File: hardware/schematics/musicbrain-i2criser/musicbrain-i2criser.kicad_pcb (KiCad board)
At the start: 2 copper layers, 28 x 80 mm, 2 parts, among them J1 BUS, J2 NAAR FRONT

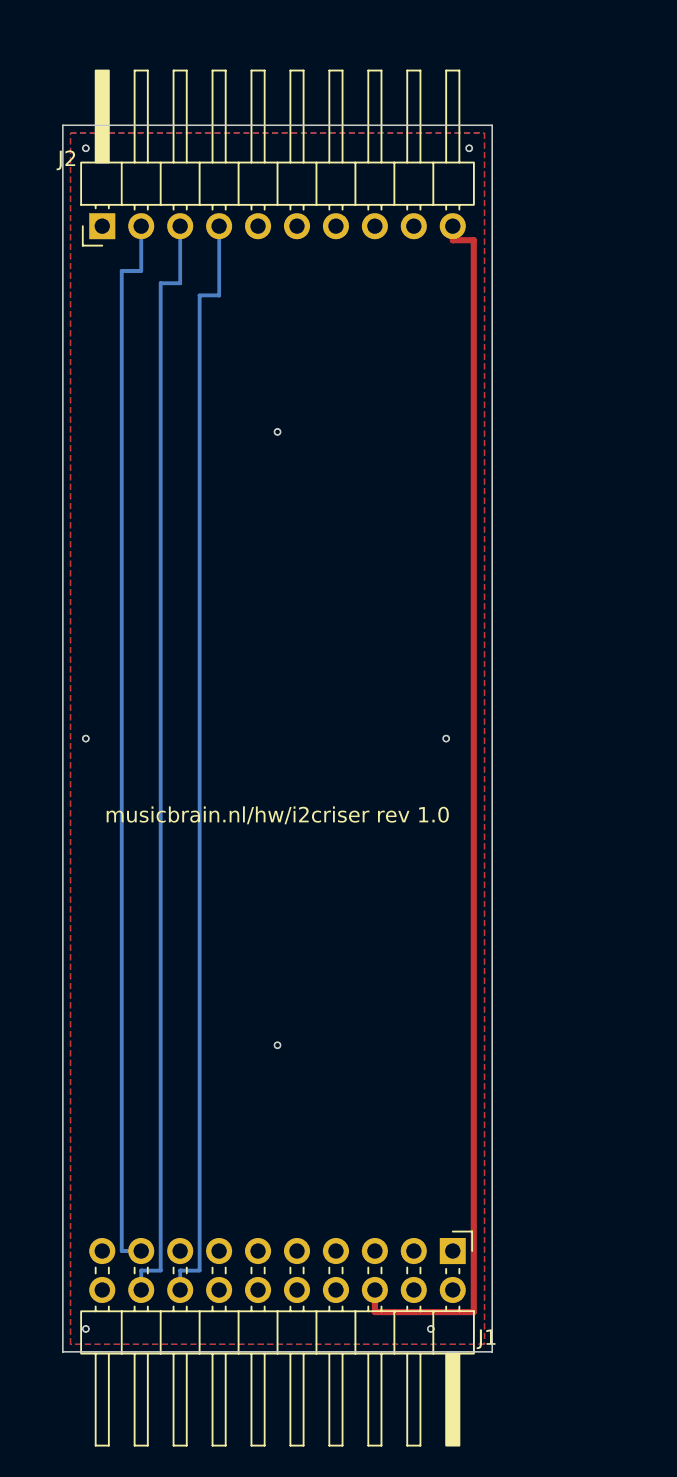
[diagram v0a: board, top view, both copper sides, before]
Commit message: Gen 2 stap 2+3a: bus.py + i2criser rev 2.0 (2x12, H=50) DRC 0/0
bus.py = één bron van waarheid voor bus-generatie 2 (spiegel van
spi-bus-spec v2.0): H=50, kaartbreedte 80, slotsteek 20,32, de 24-pins
SLOT-map, de 2x12-footprints en de front-standaard. Generators tikken de
pinout niet meer zelf over.

i2criser rev 2.0 = eerste bord op gen 2 (dom = snelste validatie van de
keten): 40x50 (de 2x12 spant 27,94 -> 28 mm was te smal), J1 2x12, J2 1x10
ongewijzigd. Routing-les: laan-volgorde is kritisch (SDA komt van de kolom
waar SCL naartoe moet -> SDA jogt meteen westwaarts); +3V3 gebruikt de
4 mm vrije strook zuid van J1 i.p.v. de krappe rijcorridor.
ERC 0 / netcheck OK / DRC 0/0.

Co-Authored-By: Claude Fable 5 <noreply@anthropic.com>
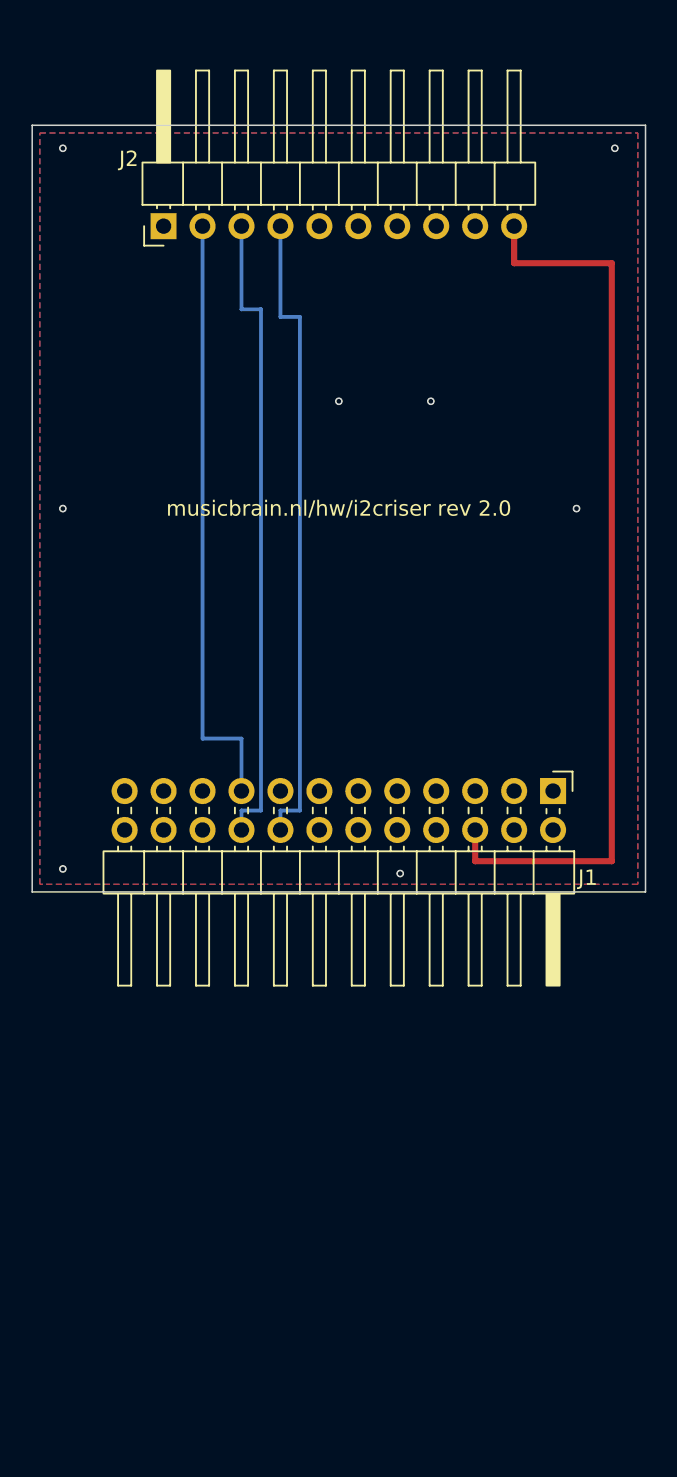
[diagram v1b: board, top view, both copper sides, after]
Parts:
- J1: footprint Connector_PinHeader_2.54mm:PinHeader_2x10_P2.54mm_Horizontal -> Connector_PinHeader_2.54mm:PinHeader_2x12_P2.54mm_Horizontal
- moved J1 30.7 mm to (134.0, 143.4)
- moved J2 4.00 mm to (108.6, 106.6)
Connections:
- J1 pad 20: (no net) -> GND
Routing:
- net /SCL: track 71.9 -> 41.9 mm
- net /IRQ: track 71.9 -> 41.9 mm
- net /SDA: track 69.4 -> 39.4 mm
- net +3V3: track 80.1 -> 58.7 mm
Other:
- board size 28 x 80 mm -> 40 x 50 mm
- board text added: "musicbrain.nl/hw/i2criser rev 2.0"
- board text removed: "musicbrain.nl/hw/i2criser rev 1.0"

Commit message: Release-archief rel-v0.2 per bord + paneel-inzet-fix (vondst Mark)
rel-v0.2/: de laatste gen-1-stand (2x10, H=80) van elk bord als bevroren
map naast de levende bestanden — KiCad-bronnen, README, overzicht, widget,
pinouts, bom/cpl. Gerbers zijn regenereerbaar (12574b3). Git-tag
hw-rel-v0.2 op f9eb436 markeert dezelfde stand repo-breed; prefix-tags
(hw-/fw-/web-) zijn de monorepo-conventie voor deelreleases.

Inzet-fix: de 1-rijer paneel-header gebruikte de 2-rijer-inzet (6,58),
waardoor de body 2,54 vóór de rand eindigde en de pin maar 3,46 mm in de
front-socket greep (i.p.v. 6,0). Nu per type: bus 6,58 / paneel 4,04 —
body eindigt exact op de rand, volle pin steekt uit. Beide risers
geregenereerd + potriser gerouteerd: DRC 0/0.

Co-Authored-By: Claude Fable 5 <noreply@anthropic.com>
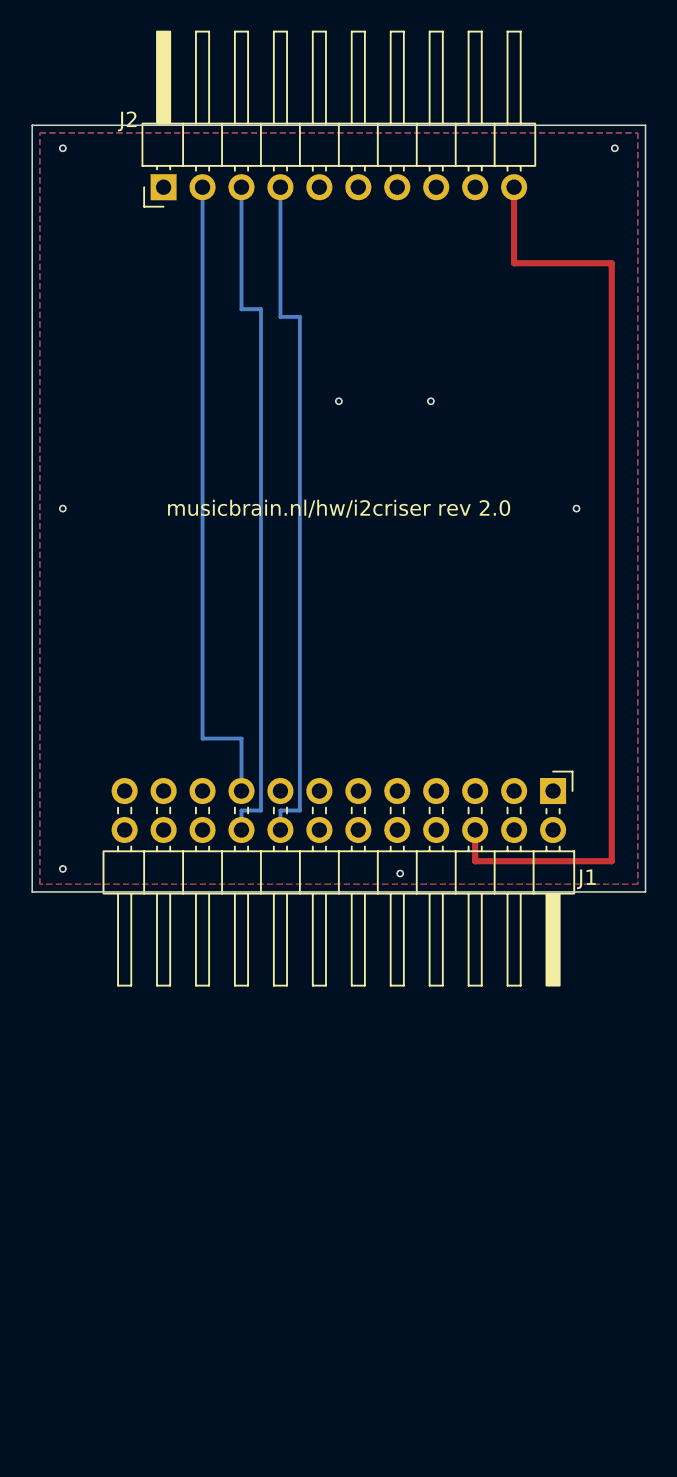
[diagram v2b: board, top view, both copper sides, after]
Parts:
- moved J2 2.54 mm to (108.6, 104.0)
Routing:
- net /SDA: track 39.4 -> 41.9 mm
- net /SCL: track 41.9 -> 44.5 mm
- net /IRQ: track 41.9 -> 44.5 mm
- net +3V3: track 58.7 -> 61.3 mm
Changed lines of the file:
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@@
   )
   (footprint "Connector_PinHeader_2.54mm:PinHeader_1x10_P2.54mm_Horizontal"
-    (at 108.57 106.58 90)
+    (at 108.57 104.04 90)
     (layer "F.Cu")
     (descr "Through hole angled pin header, 1x10, 2.54mm pitch, 6mm pin length, single row")
@@
   (segment (start 113.65 143.42) (end 113.65 140) (width 0.25) (layer "B.Cu") (net 3))
   (segment (start 113.65 140) (end 111.11 140) (width 0.25) (layer "B.Cu") (net 3))
-  (segment (start 111.11 140) (end 111.11 106.58) (width 0.25) (layer "B.Cu") (net 3))
+  (segment (start 111.11 140) (end 111.11 104.04) (width 0.25) (layer "B.Cu") (net 3))
   (segment (start 113.65 145.96) (end 113.65 144.69) (width 0.25) (layer "B.Cu") (net 4))
   (segment (start 113.65 144.69) (end 114.92 144.69) (width 0.25) (layer "B.Cu") (net 4))
   (segment (start 114.92 144.69) (end 114.92 112) (width 0.25) (layer "B.Cu") (net 4))
   (segment (start 114.92 112) (end 113.65 112) (width 0.25) (layer "B.Cu") (net 4))
-  (segment (start 113.65 112) (end 113.65 106.58) (width 0.25) (layer "B.Cu") (net 4))
+  (segment (start 113.65 112) (end 113.65 104.04) (width 0.25) (layer "B.Cu") (net 4))
   (segment (start 116.19 145.96) (end 116.19 144.69) (width 0.25) (layer "B.Cu") (net 5))
   (segment (start 116.19 144.69) (end 117.46 144.69) (width 0.25) (layer "B.Cu") (net 5))
   (segment (start 117.46 144.69) (end 117.46 112.5) (width 0.25) (layer "B.Cu") (net 5))
   (segment (start 117.46 112.5) (end 116.19 112.5) (width 0.25) (layer "B.Cu") (net 5))
-  (segment (start 116.19 112.5) (end 116.19 106.58) (width 0.25) (layer "B.Cu") (net 5))
+  (segment (start 116.19 112.5) (end 116.19 104.04) (width 0.25) (layer "B.Cu") (net 5))
   (segment (start 128.89 145.96) (end 128.89 148) (width 0.4) (layer "F.Cu") (net 2))
   (segment (start 128.89 148) (end 137.8 148) (width 0.4) (layer "F.Cu") (net 2))
   (segment (start 137.8 148) (end 137.8 109) (width 0.4) (layer "F.Cu") (net 2))
   (segment (start 137.8 109) (end 131.43 109) (width 0.4) (layer "F.Cu") (net 2))
-  (segment (start 131.43 109) (end 131.43 106.58) (width 0.4) (layer "F.Cu") (net 2))
+  (segment (start 131.43 109) (end 131.43 104.04) (width 0.4) (layer "F.Cu") (net 2))
   (via (at 102 101.5) (size 0.5) (drill 0.3) (layers "F.Cu" "B.Cu") (net 1))
   (via (at 138 101.5) (size 0.5) (drill 0.3) (layers "F.Cu" "B.Cu") (net 1))

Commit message: gen 2: kaarthoogte 50 -> 45 mm; potriser-herroute (U1 rot 270)
- bus.py: H=45 (band 30,84 mm = bewezen gen-1-dichtheid)
- gen_riser/gen_i2criser/gen_potriser: y-literals geparametriseerd op
  bus.BY0/BY1; potriser leest nu ook gnd_stitch.json in
- potriser: U1 rot 90 -> 270 (kanalen noord, SPI+GND zuid) - bij rot 90
  wikkelden de wiper-banen zich om pad 14 (AGND) en raakte die los van
  het vlak; nieuwe freerouting (0 unrouted) + 1 hechtvia
- alle drie risers: ERC 0, netcheck OK, DRC 0/0 op 40x45 (potriser 80x45)
- docs: spi-bus-spec + systeem-v3-plan H=50 -> H=45, jack4-kabelnotitie

Co-Authored-By: Claude Fable 5 <noreply@anthropic.com>
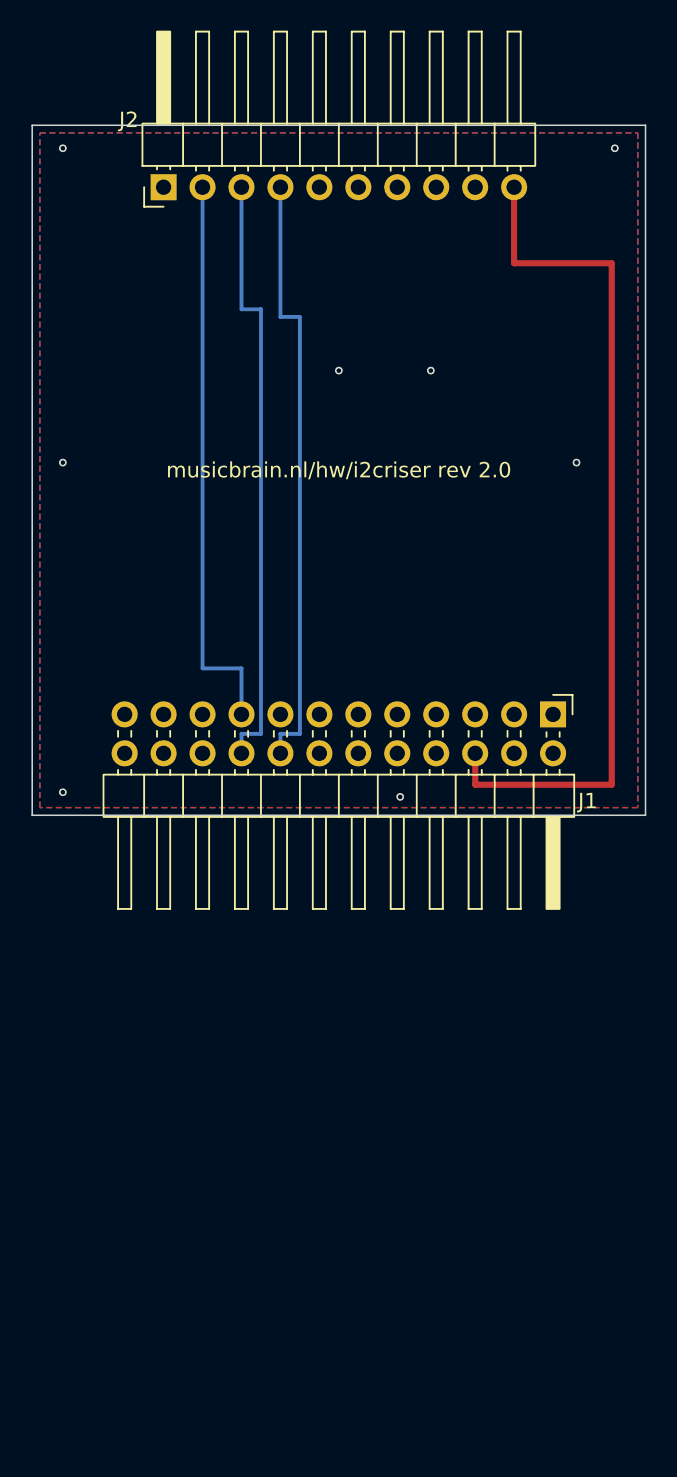
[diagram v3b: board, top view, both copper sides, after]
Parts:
- moved J1 5.00 mm to (134.0, 138.4)
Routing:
- net /SDA: track 41.9 -> 36.9 mm
- net /SCL: track 44.5 -> 39.5 mm
- net /IRQ: track 44.5 -> 39.5 mm
- net +3V3: track 61.3 -> 56.3 mm
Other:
- board size 40 x 50 mm -> 40 x 45 mm
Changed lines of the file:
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@@
   (net 5 "/IRQ")
   (footprint "Connector_PinHeader_2.54mm:PinHeader_2x12_P2.54mm_Horizontal"
-    (at 133.97 143.42 270)
+    (at 133.97 138.42 270)
     (layer "F.Cu")
     (descr "Through hole angled pin header, 2x12, 2.54mm pitch, 6mm pin length, double rows")
@@
     )
   )
-  (segment (start 113.65 143.42) (end 113.65 140) (width 0.25) (layer "B.Cu") (net 3))
-  (segment (start 113.65 140) (end 111.11 140) (width 0.25) (layer "B.Cu") (net 3))
-  (segment (start 111.11 140) (end 111.11 104.04) (width 0.25) (layer "B.Cu") (net 3))
-  (segment (start 113.65 145.96) (end 113.65 144.69) (width 0.25) (layer "B.Cu") (net 4))
-  (segment (start 113.65 144.69) (end 114.92 144.69) (width 0.25) (layer "B.Cu") (net 4))
-  (segment (start 114.92 144.69) (end 114.92 112) (width 0.25) (layer "B.Cu") (net 4))
+  (segment (start 113.65 138.42) (end 113.65 135.42) (width 0.25) (layer "B.Cu") (net 3))
+  (segment (start 113.65 135.42) (end 111.11 135.42) (width 0.25) (layer "B.Cu") (net 3))
+  (segment (start 111.11 135.42) (end 111.11 104.04) (width 0.25) (layer "B.Cu") (net 3))
+  (segment (start 113.65 140.96) (end 113.65 139.69) (width 0.25) (layer "B.Cu") (net 4))
+  (segment (start 113.65 139.69) (end 114.92 139.69) (width 0.25) (layer "B.Cu") (net 4))
+  (segment (start 114.92 139.69) (end 114.92 112) (width 0.25) (layer "B.Cu") (net 4))
   (segment (start 114.92 112) (end 113.65 112) (width 0.25) (layer "B.Cu") (net 4))
   (segment (start 113.65 112) (end 113.65 104.04) (width 0.25) (layer "B.Cu") (net 4))
-  (segment (start 116.19 145.96) (end 116.19 144.69) (width 0.25) (layer "B.Cu") (net 5))
-  (segment (start 116.19 144.69) (end 117.46 144.69) (width 0.25) (layer "B.Cu") (net 5))
-  (segment (start 117.46 144.69) (end 117.46 112.5) (width 0.25) (layer "B.Cu") (net 5))
+  (segment (start 116.19 140.96) (end 116.19 139.69) (width 0.25) (layer "B.Cu") (net 5))
+  (segment (start 116.19 139.69) (end 117.46 139.69) (width 0.25) (layer "B.Cu") (net 5))
+  (segment (start 117.46 139.69) (end 117.46 112.5) (width 0.25) (layer "B.Cu") (net 5))
   (segment (start 117.46 112.5) (end 116.19 112.5) (width 0.25) (layer "B.Cu") (net 5))
   (segment (start 116.19 112.5) (end 116.19 104.04) (width 0.25) (layer "B.Cu") (net 5))
-  (segment (start 128.89 145.96) (end 128.89 148) (width 0.4) (layer "F.Cu") (net 2))
-  (segment (start 128.89 148) (end 137.8 148) (width 0.4) (layer "F.Cu") (net 2))
-  (segment (start 137.8 148) (end 137.8 109) (width 0.4) (layer "F.Cu") (net 2))
+  (segment (start 128.89 140.96) (end 128.89 143) (width 0.4) (layer "F.Cu") (net 2))
+  (segment (start 128.89 143) (end 137.8 143) (width 0.4) (layer "F.Cu") (net 2))
+  (segment (start 137.8 143) (end 137.8 109) (width 0.4) (layer "F.Cu") (net 2))
   (segment (start 137.8 109) (end 131.43 109) (width 0.4) (layer "F.Cu") (net 2))
   (segment (start 131.43 109) (end 131.43 104.04) (width 0.4) (layer "F.Cu") (net 2))
   (via (at 102 101.5) (size 0.5) (drill 0.3) (layers "F.Cu" "B.Cu") (net 1))
   (via (at 138 101.5) (size 0.5) (drill 0.3) (layers "F.Cu" "B.Cu") (net 1))
-  (via (at 102 148.5) (size 0.5) (drill 0.3) (layers "F.Cu" "B.Cu") (net 1))
-  (via (at 124 148.8) (size 0.5) (drill 0.3) (layers "F.Cu" "B.Cu") (net 1))
-  (via (at 102 125) (size 0.5) (drill 0.3) (layers "F.Cu" "B.Cu") (net 1))
-  (via (at 135.5 125) (size 0.5) (drill 0.3) (layers "F.Cu" "B.Cu") (net 1))
-  (via (at 120 118) (size 0.5) (drill 0.3) (layers "F.Cu" "B.Cu") (net 1))
-  (via (at 126 118) (size 0.5) (drill 0.3) (layers "F.Cu" "B.Cu") (net 1))
-  (gr_rect (start 100.0 100.0) (end 140.0 150.0)
+  (via (at 102 143.5) (size 0.5) (drill 0.3) (layers "F.Cu" "B.Cu") (net 1))
+  (via (at 124 143.8) (size 0.5) (drill 0.3) (layers "F.Cu" "B.Cu") (net 1))
+  (via (at 102 122) (size 0.5) (drill 0.3) (layers "F.Cu" "B.Cu") (net 1))
+  (via (at 135.5 122) (size 0.5) (drill 0.3) (layers "F.Cu" "B.Cu") (net 1))
+  (via (at 120 116) (size 0.5) (drill 0.3) (layers "F.Cu" "B.Cu") (net 1))
+  (via (at 126 116) (size 0.5) (drill 0.3) (layers "F.Cu" "B.Cu") (net 1))
+  (gr_rect (start 100.0 100.0) (end 140.0 145.0)
     (stroke (width 0.1) (type default)) (fill none)
     (layer "Edge.Cuts"))
-  (gr_text "musicbrain.nl/hw/i2criser rev 2.0" (at 120 125 0) (layer "F.SilkS")
+  (gr_text "musicbrain.nl/hw/i2criser rev 2.0" (at 120 122.5 0) (layer "F.SilkS")
     (effects (font (size 1 1) (thickness 0.15))))
   (zone (net 1) (net_name "GND") (layer "F.Cu")
@@
     (polygon (pts
       (xy 100.5 100.5) (xy 139.5 100.5)
-      (xy 139.5 149.5) (xy 100.5 149.5)
+      (xy 139.5 144.5) (xy 100.5 144.5)
     ))
   )
@@
     (polygon (pts
       (xy 100.5 100.5) (xy 139.5 100.5)
-      (xy 139.5 149.5) (xy 100.5 149.5)
+      (xy 139.5 144.5) (xy 100.5 144.5)
     ))
   )
